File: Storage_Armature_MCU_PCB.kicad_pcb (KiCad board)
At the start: 4 copper layers, 319.7 x 137.4 mm, 98 parts, among them U23 RSCD06D3, U24 RSCD06D3, U25 RSCD06D3, U26 RSCD06D3, U4 TLV1117LV33DCYR

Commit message: VER1.0: сделал все питание и один измерительный канал
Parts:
- removed C65, C72: 1n, Capacitor_THT:C_Disc_D7.0mm_W2.5mm_P5.00mm
- removed C70: 330u, Capacitor_THT:CP_Radial_D10.0mm_P5.00mm
- removed D21: URB2405ZP-10WR3, MORNSUN:URB_ZP-10WR3
- removed J2: ~, Connector_Molex:Molex_Mini-Fit_Jr_5566-04A_2x02_P4.20mm_Vertical
- added C10: 56p, Capacitor_SMD:C_0805_2012Metric_Pad1.18x1.45mm_HandSolder, B.Cu at (339.4, 272.9)
- added C16: 10n, Capacitor_SMD:C_0805_2012Metric_Pad1.18x1.45mm_HandSolder, B.Cu at (347.4, 269.1)
- added C17: 22n, Capacitor_SMD:C_0805_2012Metric_Pad1.18x1.45mm_HandSolder, F.Cu at (364.9, 272.9)
- added C18: 2.2u, Capacitor_SMD:C_0805_2012Metric_Pad1.18x1.45mm_HandSolder, B.Cu at (363.9, 272.9)
- added C19: 100n, Capacitor_SMD:C_0805_2012Metric_Pad1.18x1.45mm_HandSolder, B.Cu at (361.6, 272.9)
- added C22: 100n, Capacitor_SMD:C_0805_2012Metric_Pad1.18x1.45mm_HandSolder, B.Cu at (351.1, 272.9)
- added C23: 2.2u, Capacitor_SMD:C_0805_2012Metric_Pad1.18x1.45mm_HandSolder, B.Cu at (348.9, 272.9)
- added C3: 10n, Capacitor_SMD:C_0805_2012Metric_Pad1.18x1.45mm_HandSolder, B.Cu at (347.4, 276.4)
- added C35: 10u, Capacitor_SMD:C_1206_3216Metric_Pad1.33x1.80mm_HandSolder, F.Cu at (377.0, 290.0)
- added C4: 100n, Capacitor_SMD:C_0805_2012Metric_Pad1.18x1.45mm_HandSolder, B.Cu at (343.4, 272.9)
- added C45: 10u, Capacitor_SMD:C_1206_3216Metric_Pad1.33x1.80mm_HandSolder, F.Cu at (364.2, 290.2)
- added C71: 4.7u, Capacitor_SMD:C_1206_3216Metric_Pad1.33x1.80mm_HandSolder, F.Cu at (354.0, 292.5)
- added C73: 4.7u, Capacitor_SMD:C_1206_3216Metric_Pad1.33x1.80mm_HandSolder, F.Cu at (350.0, 294.0)
- added C74: 10u, Capacitor_SMD:C_1206_3216Metric_Pad1.33x1.80mm_HandSolder, F.Cu at (367.0, 290.2)
- added C75: 47u, Capacitor_SMD:CP_Elec_8x6.2, F.Cu at (344.0, 288.2)
- added D1: B2405S-1WR3, MORNSUN:B_S-1WR3, F.Cu at (356.5, 289.4)
- added D10: SMCJ33A, Diode_SMD:D_SMC_Handsoldering, F.Cu at (119.2, 247.6)
- added D2: ~, Package_TO_SOT_SMD:SOT-23, F.Cu at (339.2, 276.4)
- added D23: ~, LED_SMD:LED_0805_2012Metric, F.Cu at (372.2, 294.8)
- added D9: WRB2403S-3WR2, MORNSUN:WRB_S-3WR2, F.Cu at (123.6, 235.9)
- added J28: ~, Connector_Molex:Molex_Mini-Fit_Jr_5569-02A2_2x01_P4.20mm_Horizontal, F.Cu at (369.4, 260.1)
- added J35: ~, Connector_Molex:Molex_Mini-Fit_Jr_5566-04A_2x02_P4.20mm_Vertical, F.Cu at (174.8, 252.5)
- added L2: 6.8u, Inductor_SMD:L_1210_3225Metric_Pad1.42x2.65mm_HandSolder, F.Cu at (354.0, 296.0)
- added R10: 120, Resistor_SMD:R_0805_2012Metric_Pad1.20x1.40mm_HandSolder, F.Cu at (339.4, 272.9)
- added R11: 10k, Resistor_SMD:R_0805_2012Metric_Pad1.20x1.40mm_HandSolder, F.Cu at (347.4, 271.6)
- added R21: 20k, Resistor_SMD:R_0805_2012Metric_Pad1.20x1.40mm_HandSolder, F.Cu at (347.4, 269.1)
- added R3: 10, Resistor_SMD:R_1206_3216Metric_Pad1.30x1.75mm_HandSolder, F.Cu at (366.6, 264.6)
- added R5: 20k, Resistor_SMD:R_0805_2012Metric_Pad1.20x1.40mm_HandSolder, F.Cu at (347.4, 276.4)
- added R58: 1.1k, Resistor_SMD:R_0805_2012Metric_Pad1.20x1.40mm_HandSolder, F.Cu at (368.5, 294.8)
- added R7: 100, Resistor_SMD:R_0805_2012Metric_Pad1.20x1.40mm_HandSolder, F.Cu at (365.4, 267.9)
- added R8: 10k, Resistor_SMD:R_0805_2012Metric_Pad1.20x1.40mm_HandSolder, F.Cu at (347.4, 274.1)
- added R9: 100, Resistor_SMD:R_0805_2012Metric_Pad1.20x1.40mm_HandSolder, F.Cu at (367.9, 267.9)
- added U2: NSI1200, Package_SO:SOIC-8_7.5x5.85mm_P1.27mm, F.Cu at (356.4, 272.9)
- added U5: ADP3338AKCZ-3.3RL7, Package_TO_SOT_SMD:SOT-223-3_TabPin2, F.Cu at (372.0, 288.2)
- added U6: OPA333, Package_TO_SOT_SMD:SOT-23-5, F.Cu at (343.4, 272.9)
- C68, C69: value 10u -> 4.7u
- D20: value ~ -> BZT52C10
- F1: value 0451002.MRL -> MF-SM075/60-2; footprint Fuse_my:SMD_2410 -> Fuse:Fuse_1812_4532Metric_Pad1.30x3.40mm_HandSolder
- J24, J25, J26, J27: footprint Connector_My:Mini-Fit_01x02_Vertical -> Connector_Molex:Molex_Mini-Fit_Jr_5569-02A2_2x01_P4.20mm_Horizontal
- L3: value ~ -> 12u; footprint Inductor_SMD:L_CommonModeChoke_Murata_DLW5BTMxxxSQ2x_5x5mm -> Inductor_SMD:L_1210_3225Metric_Pad1.42x2.65mm_HandSolder
- Q1: value ~ -> 20N06
- moved H3 156.9 mm to (377.7, 302.7)
- moved H4 156.6 mm to (377.7, 167.6)
- moved C47 105.1 mm to (264.3, 203.8)
- moved C48 105.1 mm to (261.8, 203.8)
- moved C49 105.1 mm to (248.1, 206.3)
- moved D12 105.1 mm to (255.5, 206.2)
- moved L1 105.1 mm to (241.3, 206.3)
- moved R37 105.1 mm to (244.8, 208.3)
- moved R40 105.1 mm to (244.8, 204.3)
- moved C1 99.9 mm to (416.1, 196.3)
- moved C12 99.9 mm to (416.1, 208.3)
- moved C13 99.9 mm to (420.9, 196.3)
- moved C14 99.9 mm to (420.9, 199.3)
- moved C15 99.9 mm to (420.9, 202.3)
- moved C2 99.9 mm to (416.1, 199.3)
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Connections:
- C67 pad 1: Net-(C67-Pad1) -> +24V
- C68 pad 1: Net-(C67-Pad1) -> +24V
- C69 pad 2: Net-(C69-Pad2) -> GNDD
- F1 pad 2: Net-(C67-Pad1) -> +24V
- L3 pad 1: Net-(C67-Pad1) -> +24V
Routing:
- net Net-(C16-Pad2): track 0.00 -> 18.3 mm, vias 0 -> 1
- net CAN1_TXD_MCU: track 14.0 -> 0.00 mm
- net Net-(C17-Pad1): track 0.00 -> 10.6 mm
- net GND: track 17.2 -> 27.1 mm, vias 0 -> 5
- net CAN1_RXD_MCU: track 8.00 -> 0.00 mm
- net +3.3V: track 0.00 -> 7.96 mm, vias 0 -> 3
- net /P_measure/P_OUT: track 0.00 -> 7.37 mm
- net /P_measure/P_IN: track 0.00 -> 7.37 mm
- net Net-(C17-Pad2): track 0.00 -> 6.51 mm
- net /P_measure/P_measure_MCU: track 0.00 -> 6.12 mm, vias 0 -> 1
- net Net-(U6--): track 0.00 -> 5.61 mm, vias 0 -> 1
- net Net-(U6-+): track 0.00 -> 5.36 mm, vias 0 -> 1
- net GND_ISO: track 0.00 -> 4.69 mm, vias 0 -> 1
- net +3.3V_ISO: track 0.00 -> 4.49 mm, vias 0 -> 1
- net Net-(R8-Pad1): track 0.00 -> 2.93 mm
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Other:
- board size 319.7 x 137.4 mm -> 163 x 146.1 mm
- board text added: "+3.3V ISO"
- board text added: "IN"
- board text added: "OUT"

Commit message: VER1.0: разместил все компоненты
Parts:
- removed C75: 47u, Capacitor_SMD:CP_Elec_8x6.2
- removed D15: ~, Package_TO_SOT_SMD:SOT-23-3
- removed H1: MountingHole_Pad, MountingHole:MountingHole_4.3mm_M4_Pad_Via
- added C11: 56p, Capacitor_SMD:C_0805_2012Metric_Pad1.18x1.45mm_HandSolder, B.Cu at (339.2, 246.2)
- added C24: 2.2u, Capacitor_SMD:C_0805_2012Metric_Pad1.18x1.45mm_HandSolder, B.Cu at (363.8, 246.2)
- added C25: 100n, Capacitor_SMD:C_0805_2012Metric_Pad1.18x1.45mm_HandSolder, B.Cu at (361.5, 246.2)
- added C27: 22n, Capacitor_SMD:C_0805_2012Metric_Pad1.18x1.45mm_HandSolder, F.Cu at (364.8, 246.2)
- added C28: 100n, Capacitor_SMD:C_0805_2012Metric_Pad1.18x1.45mm_HandSolder, B.Cu at (351.0, 246.2)
- added C29: 2.2u, Capacitor_SMD:C_0805_2012Metric_Pad1.18x1.45mm_HandSolder, B.Cu at (348.8, 246.2)
- added C31: 10n, Capacitor_SMD:C_0805_2012Metric_Pad1.18x1.45mm_HandSolder, B.Cu at (347.2, 242.4)
- added C32: 2.2u, Capacitor_SMD:C_0805_2012Metric_Pad1.18x1.45mm_HandSolder, B.Cu at (363.8, 219.7)
- added C33: 100n, Capacitor_SMD:C_0805_2012Metric_Pad1.18x1.45mm_HandSolder, B.Cu at (361.5, 219.7)
- added C36: 22n, Capacitor_SMD:C_0805_2012Metric_Pad1.18x1.45mm_HandSolder, F.Cu at (364.8, 219.7)
- added C37: 100n, Capacitor_SMD:C_0805_2012Metric_Pad1.18x1.45mm_HandSolder, B.Cu at (351.0, 219.7)
- added C38: 2.2u, Capacitor_SMD:C_0805_2012Metric_Pad1.18x1.45mm_HandSolder, B.Cu at (348.8, 219.7)
- added C39: 10n, Capacitor_SMD:C_0805_2012Metric_Pad1.18x1.45mm_HandSolder, B.Cu at (347.2, 215.9)
- added C40: 100n, Capacitor_SMD:C_0805_2012Metric_Pad1.18x1.45mm_HandSolder, B.Cu at (343.2, 219.7)
- added C41: 56p, Capacitor_SMD:C_0805_2012Metric_Pad1.18x1.45mm_HandSolder, B.Cu at (339.2, 219.7)
- added C42: 2.2u, Capacitor_SMD:C_0805_2012Metric_Pad1.18x1.45mm_HandSolder, B.Cu at (363.8, 193.1)
- added C43: 100n, Capacitor_SMD:C_0805_2012Metric_Pad1.18x1.45mm_HandSolder, B.Cu at (361.5, 193.1)
- added C46: 22n, Capacitor_SMD:C_0805_2012Metric_Pad1.18x1.45mm_HandSolder, F.Cu at (364.8, 193.1)
- added C5: 10n, Capacitor_SMD:C_0805_2012Metric_Pad1.18x1.45mm_HandSolder, B.Cu at (347.2, 249.7)
- added C50: 100n, Capacitor_SMD:C_0805_2012Metric_Pad1.18x1.45mm_HandSolder, B.Cu at (351.0, 193.1)
- added C51: 2.2u, Capacitor_SMD:C_0805_2012Metric_Pad1.18x1.45mm_HandSolder, B.Cu at (348.8, 193.1)
- added C52: 10n, Capacitor_SMD:C_0805_2012Metric_Pad1.18x1.45mm_HandSolder, B.Cu at (347.2, 196.6)
- added C53: 10n, Capacitor_SMD:C_0805_2012Metric_Pad1.18x1.45mm_HandSolder, B.Cu at (347.2, 189.3)
- added C54: 100n, Capacitor_SMD:C_0805_2012Metric_Pad1.18x1.45mm_HandSolder, B.Cu at (343.2, 193.1)
- added C55: 56p, Capacitor_SMD:C_0805_2012Metric_Pad1.18x1.45mm_HandSolder, B.Cu at (339.2, 193.1)
- added C56: 2.2u, Capacitor_SMD:C_0805_2012Metric_Pad1.18x1.45mm_HandSolder, B.Cu at (363.8, 166.6)
- added C57: 100n, Capacitor_SMD:C_0805_2012Metric_Pad1.18x1.45mm_HandSolder, B.Cu at (361.5, 166.6)
- added C58: 22n, Capacitor_SMD:C_0805_2012Metric_Pad1.18x1.45mm_HandSolder, F.Cu at (364.8, 166.6)
- added C59: 100n, Capacitor_SMD:C_0805_2012Metric_Pad1.18x1.45mm_HandSolder, B.Cu at (351.0, 166.6)
- added C6: 100n, Capacitor_SMD:C_0805_2012Metric_Pad1.18x1.45mm_HandSolder, B.Cu at (343.2, 246.2)
- added C60: 2.2u, Capacitor_SMD:C_0805_2012Metric_Pad1.18x1.45mm_HandSolder, B.Cu at (348.8, 166.6)
- added C61: 10n, Capacitor_SMD:C_0805_2012Metric_Pad1.18x1.45mm_HandSolder, B.Cu at (347.2, 170.1)
- added C62: 10n, Capacitor_SMD:C_0805_2012Metric_Pad1.18x1.45mm_HandSolder, B.Cu at (347.2, 162.8)
- added C63: 100n, Capacitor_SMD:C_0805_2012Metric_Pad1.18x1.45mm_HandSolder, B.Cu at (343.2, 166.6)
- added C64: 56p, Capacitor_SMD:C_0805_2012Metric_Pad1.18x1.45mm_HandSolder, B.Cu at (339.2, 166.6)
- added C65: 100n, Capacitor_SMD:C_0805_2012Metric_Pad1.18x1.45mm_HandSolder, B.Cu at (313.5, 205.2)
- added C7: 10n, Capacitor_SMD:C_0805_2012Metric_Pad1.18x1.45mm_HandSolder, B.Cu at (347.2, 223.2)
- added D3: ~, Package_TO_SOT_SMD:SOT-23, F.Cu at (339.1, 249.8)
- added D4: ~, Package_TO_SOT_SMD:SOT-23, F.Cu at (339.1, 223.2)
- added D6: ~, Package_TO_SOT_SMD:SOT-23, F.Cu at (339.1, 196.7)
- added D8: ~, Package_TO_SOT_SMD:SOT-23, F.Cu at (339.1, 170.1)
- added H5: MountingHole, MountingHole:MountingHole_4.3mm_M4, F.Cu at (225.8, 302.5)
- added J29: ~, Connector_Molex:Molex_Mini-Fit_Jr_5569-02A2_2x01_P4.20mm_Horizontal, F.Cu at (369.2, 233.4)
- added J30: ~, Connector_Molex:Molex_Mini-Fit_Jr_5569-02A2_2x01_P4.20mm_Horizontal, F.Cu at (369.2, 206.9)
- added J31: ~, Connector_Molex:Molex_Mini-Fit_Jr_5569-02A2_2x01_P4.20mm_Horizontal, F.Cu at (369.2, 180.3)
- added J32: ~, Connector_Molex:Molex_Mini-Fit_Jr_5569-02A2_2x01_P4.20mm_Horizontal, F.Cu at (369.2, 153.8)
- added R12: 100, Resistor_SMD:R_0805_2012Metric_Pad1.20x1.40mm_HandSolder, F.Cu at (367.8, 241.2)
- added R13: 100, Resistor_SMD:R_0805_2012Metric_Pad1.20x1.40mm_HandSolder, F.Cu at (365.2, 241.2)
- added R14: 10k, Resistor_SMD:R_0805_2012Metric_Pad1.20x1.40mm_HandSolder, F.Cu at (347.2, 247.4)
- added R15: 10k, Resistor_SMD:R_0805_2012Metric_Pad1.20x1.40mm_HandSolder, F.Cu at (347.2, 244.9)
- added R16: 20k, Resistor_SMD:R_0805_2012Metric_Pad1.20x1.40mm_HandSolder, F.Cu at (347.2, 249.7)
- added R17: 120, Resistor_SMD:R_0805_2012Metric_Pad1.20x1.40mm_HandSolder, F.Cu at (339.2, 246.2)
- added R18: 10, Resistor_SMD:R_1206_3216Metric_Pad1.30x1.75mm_HandSolder, F.Cu at (366.5, 211.4)
- added R19: 100, Resistor_SMD:R_0805_2012Metric_Pad1.20x1.40mm_HandSolder, F.Cu at (367.8, 214.7)
- added R20: 100, Resistor_SMD:R_0805_2012Metric_Pad1.20x1.40mm_HandSolder, F.Cu at (365.2, 214.7)
- added R22: 20k, Resistor_SMD:R_0805_2012Metric_Pad1.20x1.40mm_HandSolder, F.Cu at (347.2, 242.4)
- added R23: 10k, Resistor_SMD:R_0805_2012Metric_Pad1.20x1.40mm_HandSolder, F.Cu at (347.2, 220.9)
- added R24: 10k, Resistor_SMD:R_0805_2012Metric_Pad1.20x1.40mm_HandSolder, F.Cu at (347.2, 218.4)
- added R25: 20k, Resistor_SMD:R_0805_2012Metric_Pad1.20x1.40mm_HandSolder, F.Cu at (347.2, 223.2)
- added R26: 20k, Resistor_SMD:R_0805_2012Metric_Pad1.20x1.40mm_HandSolder, F.Cu at (347.2, 215.9)
- added R27: 120, Resistor_SMD:R_0805_2012Metric_Pad1.20x1.40mm_HandSolder, F.Cu at (339.2, 219.7)
- added R28: 10, Resistor_SMD:R_1206_3216Metric_Pad1.30x1.75mm_HandSolder, F.Cu at (366.5, 184.8)
- added R29: 100, Resistor_SMD:R_0805_2012Metric_Pad1.20x1.40mm_HandSolder, F.Cu at (367.8, 188.1)
- added R30: 100, Resistor_SMD:R_0805_2012Metric_Pad1.20x1.40mm_HandSolder, F.Cu at (365.2, 188.1)
- added R31: 10k, Resistor_SMD:R_0805_2012Metric_Pad1.20x1.40mm_HandSolder, F.Cu at (347.2, 194.3)
- added R32: 10k, Resistor_SMD:R_0805_2012Metric_Pad1.20x1.40mm_HandSolder, F.Cu at (347.2, 191.8)
- added R33: 20k, Resistor_SMD:R_0805_2012Metric_Pad1.20x1.40mm_HandSolder, F.Cu at (347.2, 196.6)
- added R34: 20k, Resistor_SMD:R_0805_2012Metric_Pad1.20x1.40mm_HandSolder, F.Cu at (347.2, 189.3)
- added R35: 120, Resistor_SMD:R_0805_2012Metric_Pad1.20x1.40mm_HandSolder, F.Cu at (339.2, 193.1)
- added R36: 10, Resistor_SMD:R_1206_3216Metric_Pad1.30x1.75mm_HandSolder, F.Cu at (366.5, 158.3)
- added R38: 100, Resistor_SMD:R_0805_2012Metric_Pad1.20x1.40mm_HandSolder, F.Cu at (367.8, 161.6)
- added R4: 10, Resistor_SMD:R_1206_3216Metric_Pad1.30x1.75mm_HandSolder, F.Cu at (366.5, 237.9)
- added R41: 100, Resistor_SMD:R_0805_2012Metric_Pad1.20x1.40mm_HandSolder, F.Cu at (365.2, 161.6)
- added R42: 10k, Resistor_SMD:R_0805_2012Metric_Pad1.20x1.40mm_HandSolder, F.Cu at (347.2, 167.8)
- added R43: 10k, Resistor_SMD:R_0805_2012Metric_Pad1.20x1.40mm_HandSolder, F.Cu at (347.2, 165.3)
- added R44: 20k, Resistor_SMD:R_0805_2012Metric_Pad1.20x1.40mm_HandSolder, F.Cu at (347.2, 170.1)
- added R45: 20k, Resistor_SMD:R_0805_2012Metric_Pad1.20x1.40mm_HandSolder, F.Cu at (347.2, 162.8)
- added R46: 120, Resistor_SMD:R_0805_2012Metric_Pad1.20x1.40mm_HandSolder, F.Cu at (339.2, 166.6)
- added R47: 20, Resistor_SMD:R_0805_2012Metric_Pad1.20x1.40mm_HandSolder, F.Cu at (283.8, 202.2)
- added R48: 20, Resistor_SMD:R_0805_2012Metric_Pad1.20x1.40mm_HandSolder, F.Cu at (283.8, 204.8)
- added U10: NSI1200, Package_SO:SOIC-8_7.5x5.85mm_P1.27mm, F.Cu at (356.2, 193.1)
- added U11: OPA333, Package_TO_SOT_SMD:SOT-23-5, F.Cu at (343.2, 193.1)
- added U12: NSI1200, Package_SO:SOIC-8_7.5x5.85mm_P1.27mm, F.Cu at (356.2, 166.6)
- added U13: OPA333, Package_TO_SOT_SMD:SOT-23-5, F.Cu at (343.2, 166.6)
- added U14: USBLC6-2P6, Package_TO_SOT_SMD:SOT-23-6, F.Cu at (288.2, 203.5)
- added U3: NSI1200, Package_SO:SOIC-8_7.5x5.85mm_P1.27mm, F.Cu at (356.2, 246.2)
- added U7: OPA333, Package_TO_SOT_SMD:SOT-23-5, F.Cu at (343.2, 246.2)
- added U8: NSI1200, Package_SO:SOIC-8_7.5x5.85mm_P1.27mm, F.Cu at (356.2, 219.7)
- added U9: OPA333, Package_TO_SOT_SMD:SOT-23-5, F.Cu at (343.2, 219.7)
- C1, C12, C13, C14, C15, C2, C20, C21, C8, C9, R6: moved to B.Cu
- F1: footprint Fuse:Fuse_1812_4532Metric_Pad1.30x3.40mm_HandSolder -> Fuse:Fuse_Bourns_MF-SM_7.98x5.44mm
- H4: value MountingHole_Pad -> MountingHole; footprint MountingHole:MountingHole_4.3mm_M4_Pad_Via -> MountingHole:MountingHole_4.3mm_M4
- J34, J35, J6: footprint Connector_Molex:Molex_Mini-Fit_Jr_5566-04A_2x02_P4.20mm_Vertical -> Connector_Molex:Molex_Mini-Fit_Jr_5569-04A2_2x02_P4.20mm_Horizontal
- L3: value 12u -> 6.8u
- R1, R2: value 1k -> 10k; moved to B.Cu
- U4: value TLV1117LV33DCYR -> ADP3338AKCZ-3.3RL7
- moved D10 131.1 mm to (245.8, 213.3), turned to -90 degrees
- moved J1 129.9 mm to (280.0, 207.3)
- moved U1 128.8 mm to (301.8, 199.8), turned to 180 degrees
- moved D9 126.4 mm to (250.0, 237.4)
- moved D7 126.3 mm to (309.2, 209.2), turned to 90 degrees
- moved R1 124.9 mm to (301.0, 205.0), turned to -90 degrees
- moved C21 124.6 mm to (296.5, 203.0)
- moved C20 122.9 mm to (298.5, 194.5), turned to -90 degrees
- moved C30 120.9 mm to (317.8, 202.5), turned to 0 degrees
- moved C2 120.0 mm to (296.2, 194.5), turned to -90 degrees
- moved C8 119.7 mm to (296.5, 205.2)
- moved C13 118.0 mm to (303.2, 205.0), turned to 90 degrees
- moved Y1 117.0 mm to (317.8, 206.0), turned to -90 degrees
- moved R6 116.7 mm to (309.2, 209.2), turned to 90 degrees
- moved C14 114.2 mm to (306.8, 202.0), turned to 180 degrees
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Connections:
- net /P_measure/P_IN renamed /Sensor_1/P_IN
- net /P_measure/P_OUT renamed /Sensor_1/P_OUT
- net /P_measure/P_measure_MCU renamed /Sensor_1/P_measure_MCU
- net CANH renamed /CANH
- net CANL renamed /CANL
- D12 pad 1: CAN1_RXD_MCU -> /CAN_RXD_MCU
- D12 pad 2: CAN1_TXD_MCU -> /CAN_TXD_MCU
- J1 pad 2: /SWCLK -> Net-(J1-Pin_2)
- J1 pad 3: /SWDIO -> Net-(J1-Pin_3)
- U1 pad 44: unconnected-(U1-PA11-Pad44) -> /CAN_RXD_MCU
- U1 pad 45: unconnected-(U1-PA12-Pad45) -> /CAN_TXD_MCU
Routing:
- net GND: track 27.1 -> 66.9 mm, vias 5 -> 25
- net +3.3V: track 7.96 -> 39.8 mm, vias 3 -> 15
- net GND_ISO: track 4.69 -> 23.4 mm, vias 1 -> 5
- net Net-(C53-Pad2): track 0.00 -> 18.3 mm, vias 0 -> 1
- net Net-(C31-Pad2): track 0.00 -> 18.3 mm, vias 0 -> 1
- net Net-(C62-Pad2): track 0.00 -> 18.3 mm, vias 0 -> 1
- net Net-(C39-Pad2): track 0.00 -> 18.3 mm, vias 0 -> 1
- net +3.3V_ISO: track 4.49 -> 22.4 mm, vias 1 -> 5
- net Net-(C17-Pad1): track 10.6 -> 2.77 mm
- net /Sensor_1/P_OUT: track 7.37 -> 0.00 mm
- net /Sensor_1/P_IN: track 7.37 -> 0.00 mm
- net /Sensor_4/P_measure_MCU: track 0.00 -> 6.12 mm, vias 0 -> 1
- net /Sensor_2/P_measure_MCU: track 0.00 -> 6.12 mm, vias 0 -> 1
- net /Sensor_3/P_measure_MCU: track 0.00 -> 6.12 mm, vias 0 -> 1
- net /Sensor_5/P_measure_MCU: track 0.00 -> 6.12 mm, vias 0 -> 1
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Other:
- board size 163 x 146.1 mm -> 163 x 170 mm
- board text added: "+"
- board text added: "-"
- board text added: "CANH"
- board text added: "CANL"
- board text added: "CGND"

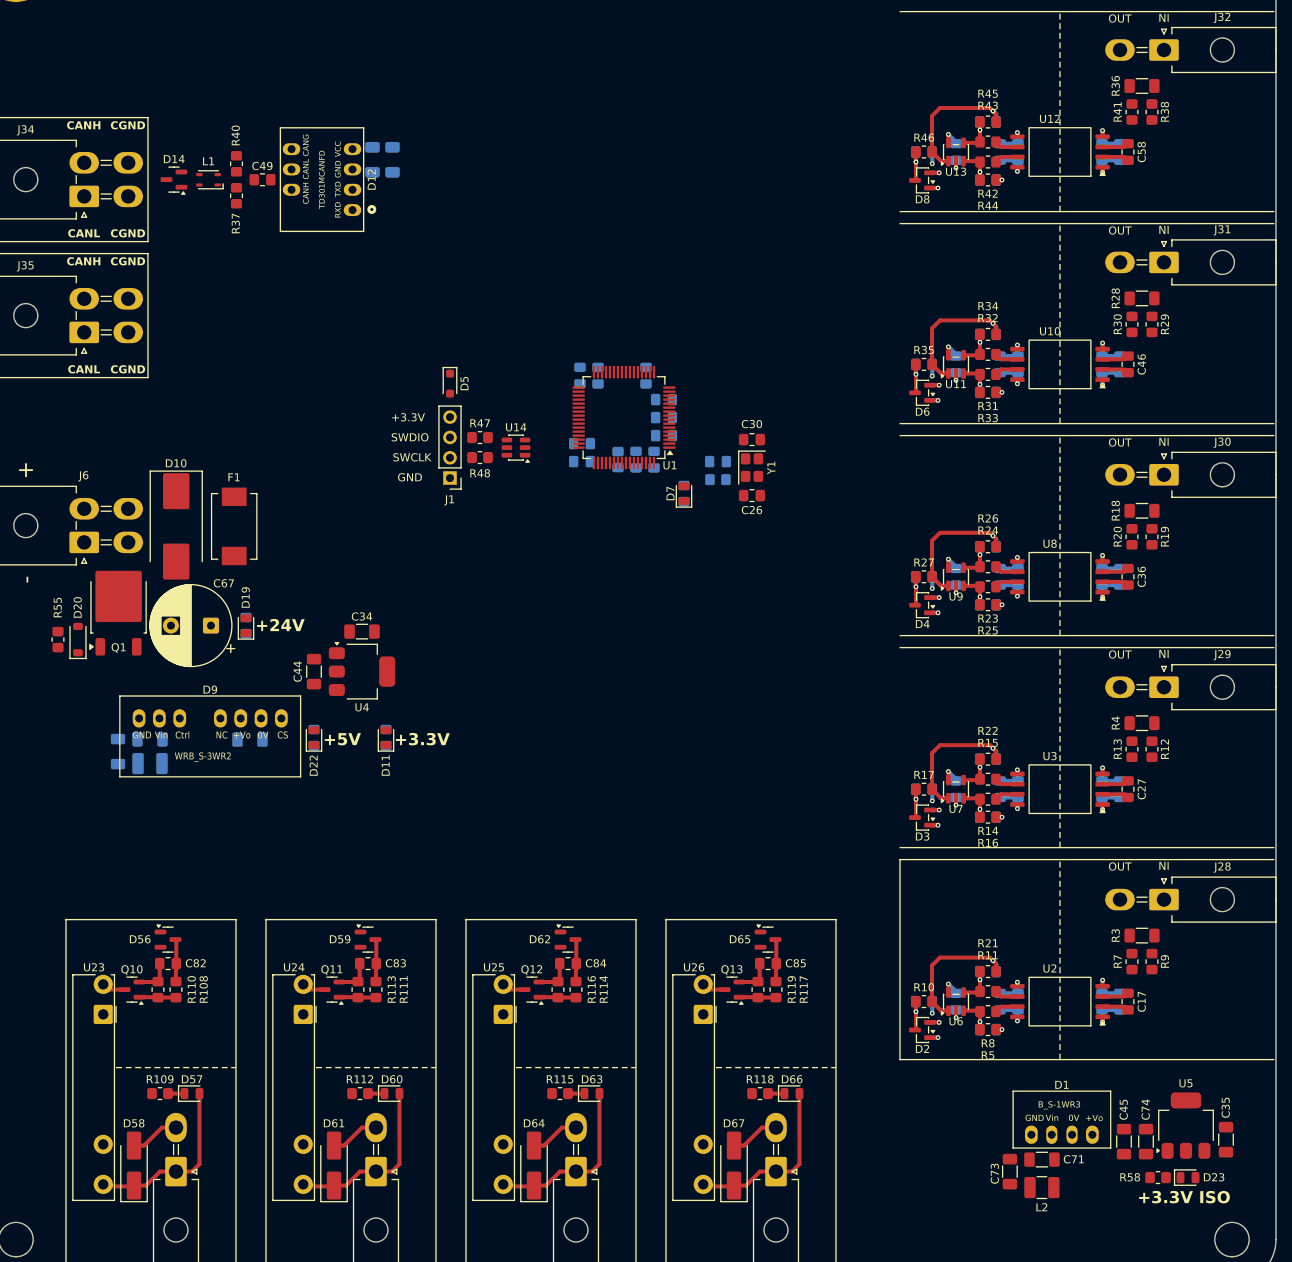
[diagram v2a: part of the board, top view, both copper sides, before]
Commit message: VER1.0: развел все кроме ножек МК
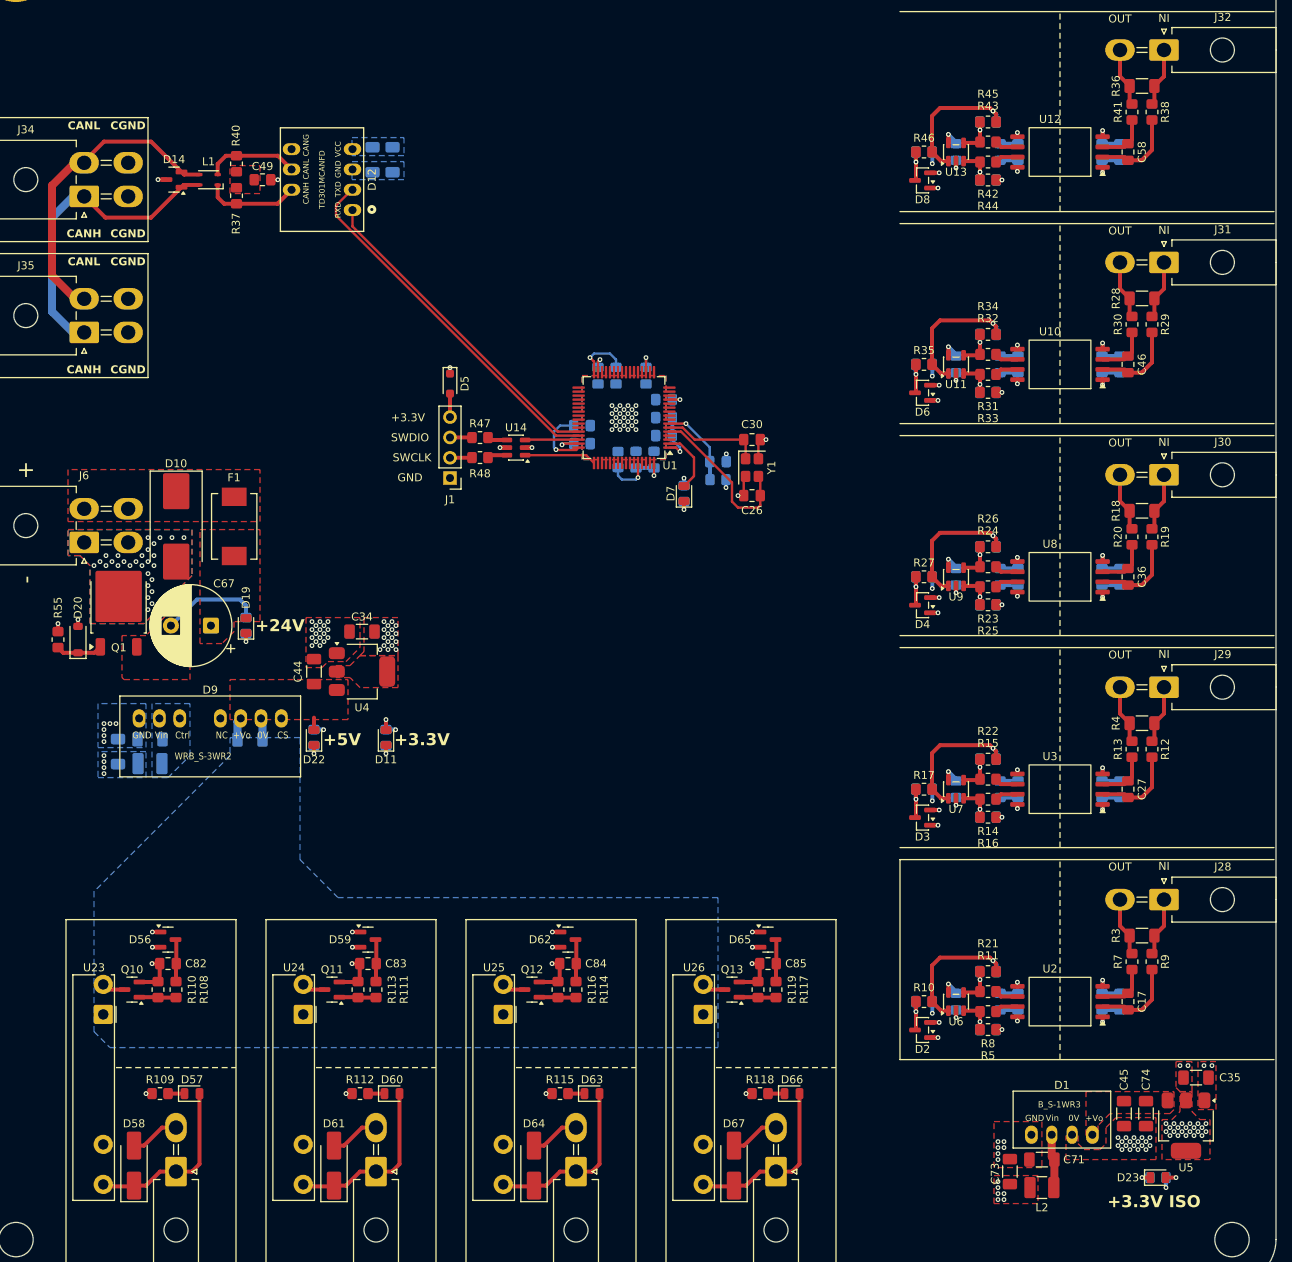
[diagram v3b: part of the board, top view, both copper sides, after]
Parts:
- R58: moved to B.Cu
- moved C35 8.61 mm to (373.2, 282.2), turned to 180 degrees
- moved C2 4.50 mm to (300.8, 194.5)
- moved C8 4.50 mm to (296.5, 200.8)
- moved D23 3.75 mm to (368.5, 294.8)
- moved C45 3.50 mm to (364.2, 286.8), turned to 90 degrees
- moved C74 3.50 mm to (367.0, 286.8), turned to -90 degrees
- turned R58 to 0 degrees
- turned U5 to -90 degrees
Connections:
- net -24V renamed -24V_IN
- D10 pad 1: +24V -> +24_IN
- F1 pad 1: +24V -> +24_IN
- J24 pad 1: GNDD -> Net-(D57-A)
- J24 pad 2: Net-(D57-A) -> GNDD
- J25 pad 1: GNDD -> Net-(D60-A)
- J25 pad 2: Net-(D60-A) -> GNDD
- J26 pad 1: GNDD -> Net-(D63-A)
- J26 pad 2: Net-(D63-A) -> GNDD
- J27 pad 1: GNDD -> Net-(D66-A)
- J27 pad 2: Net-(D66-A) -> GNDD
- J34 pad 1: /CANL -> /CANH
- J34 pad 2: /CANH -> /CANL
- J35 pad 1: /CANL -> /CANH
- J35 pad 2: /CANH -> /CANL
- J6 pad 2: +24V -> +24_IN
- J6 pad 4: +24V -> +24_IN
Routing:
- net /CAN_TXD_MCU: track 0.00 -> 45.8 mm
- net /CAN_RXD_MCU: track 0.00 -> 40.9 mm
- net /CANH: track 0.00 -> 39.2 mm
- net +3.3V: track 39.8 -> 78.9 mm, vias 15 -> 46
- net /CANL: track 0.00 -> 39.0 mm
- net GND: track 66.9 -> 89.1 mm, vias 25 -> 82
- net Net-(U1-PH0): track 0.00 -> 20.5 mm
- net GNDD: track 24.7 -> 41.1 mm, vias 0 -> 17
- net Net-(U1-PH1): track 0.00 -> 12.4 mm
- net Net-(D12-CANH): track 0.00 -> 11.8 mm
- net Net-(D12-CANL): track 0.00 -> 11.7 mm
- net NRST: track 0.00 -> 10.3 mm, vias 0 -> 1
- net /SWCLK: track 0.00 -> 9.02 mm
- net Net-(D7-A): track 0.00 -> 7.88 mm
- net /Sensor_4/P_OUT: track 0.00 -> 7.37 mm
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- added copper zone on B.Cu, net +24V
- added copper zone on F.Cu, net +24V
- added copper zone on In2.Cu, net +24V
- added copper zone on F.Cu, net +24_IN
- added copper zone on B.Cu, net +3.3V
- added copper zone on F.Cu, net +3.3V
- added copper zone on In2.Cu, net +3.3V
- added copper zone on F.Cu, net +3.3V_ISO
- added copper zone on In2.Cu, net +3.3V_ISO
- added copper zone on B.Cu, net +5V
- added copper zone on F.Cu, net +5V
- added copper zone on B.Cu, net -24V_IN
- added copper zone on F.Cu, net -24V_IN
- added copper zone on In1.Cu, net -24V_IN
- added copper zone on In2.Cu, net -24V_IN
- added copper zone on B.Cu, net GND
- added copper zone on F.Cu, net GND
- added copper zone on In1.Cu, net GND
- added copper zone on B.Cu, net GNDD
- added copper zone on F.Cu, net GNDD
- added copper zone on In1.Cu, net GNDD
- added copper zone on In1.Cu, net GND_CAN
- added copper zone on F.Cu, net GND_ISO
- added copper zone on In1.Cu, net GND_ISO
- added copper zone on F.Cu, net Net-(C49-Pad1)
- added copper zone on F.Cu, net Net-(D1-+Vo)
- added copper zone on B.Cu, net Net-(D9-Vin)
